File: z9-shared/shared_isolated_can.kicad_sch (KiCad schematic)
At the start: 6 parts, among them U951 ISO1042-Q1

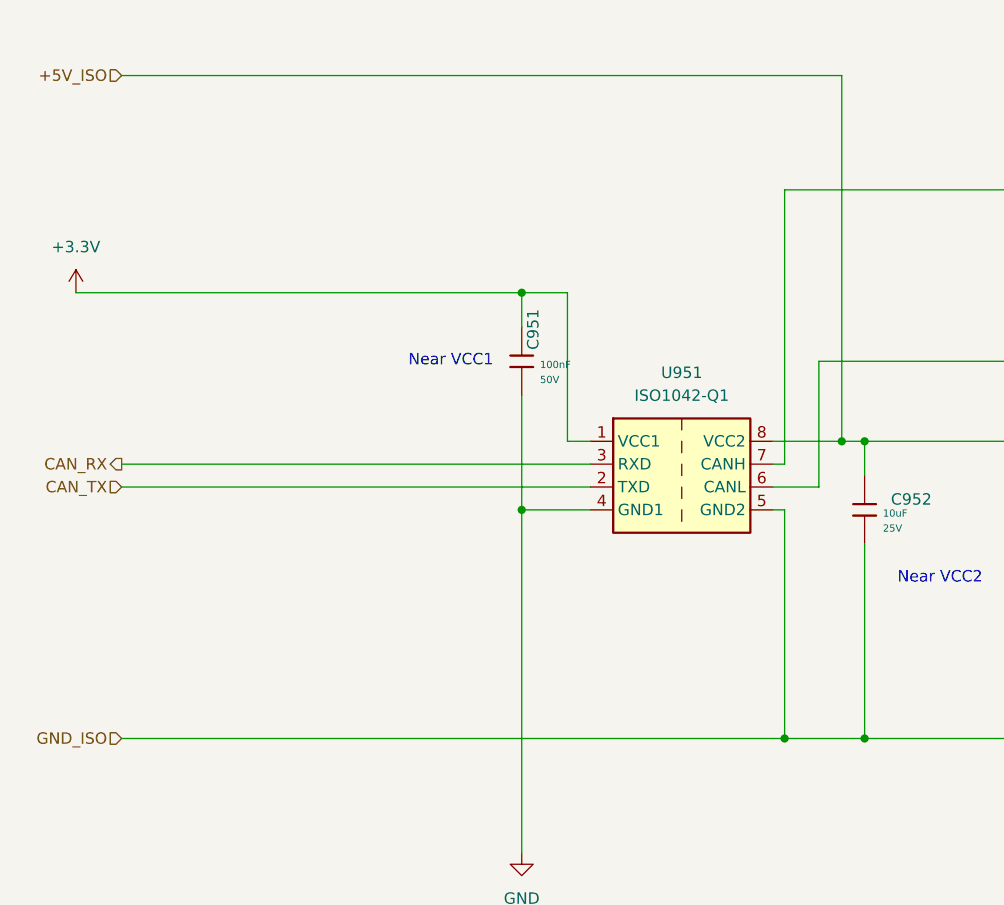
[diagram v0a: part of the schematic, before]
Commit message: Add PWR_FLAG symbols to schematic for power source indication
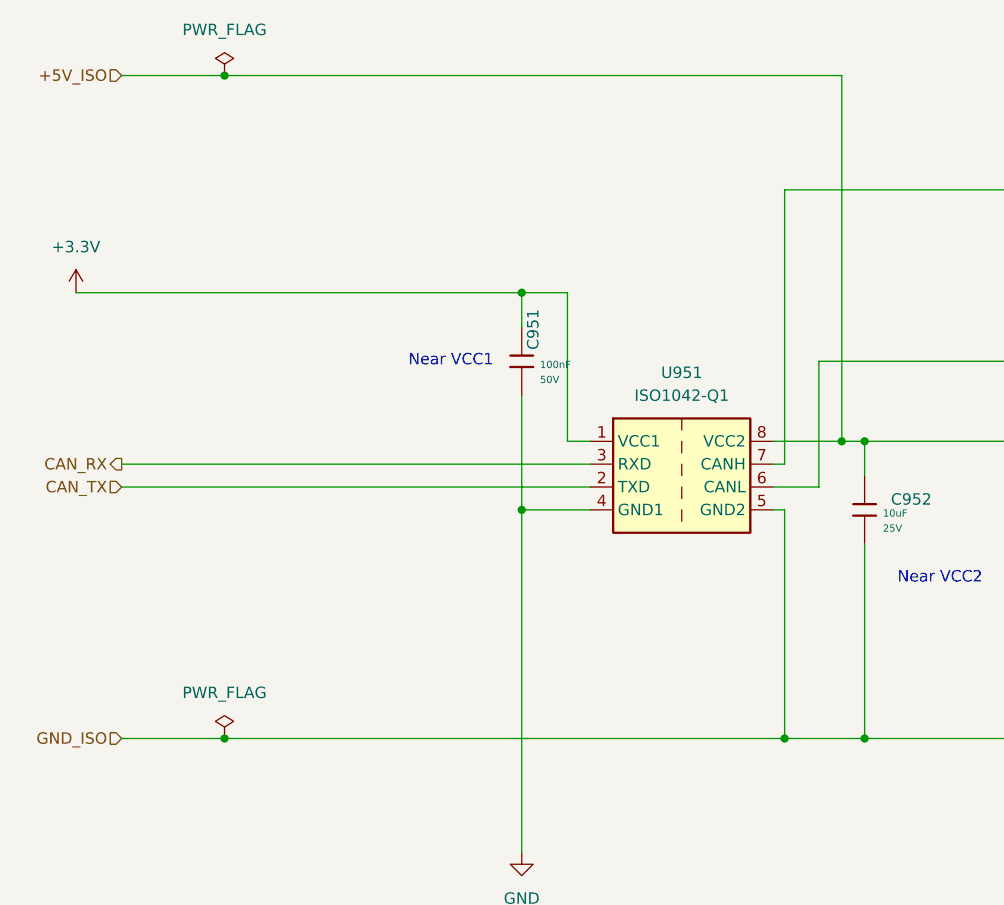
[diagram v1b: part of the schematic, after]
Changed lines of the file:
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@@
+	)
+	(junction
+		(at 95.25 49.53)
+		(diameter 0)
+		(color 0 0 0 0)
 	)
 	(junction
@@
 	)
 	(junction
+		(at 95.25 123.19)
+		(diameter 0)
+		(color 0 0 0 0)
+	)
+	(junction
 		(at 157.48 123.19)
 		(diameter 0)
@@
 	(wire
 		(pts
-			(xy 83.82 123.19) (xy 157.48 123.19)
+			(xy 95.25 49.53) (xy 163.83 49.53)
+		)
+		(stroke
+			(width 0)
+			(type default)
+		)
+	)
+	(wire
+		(pts
+			(xy 95.25 123.19) (xy 157.48 123.19)
+		)
+		(stroke
+			(width 0)
+			(type default)
+		)
+	)
+	(wire
+		(pts
+			(xy 83.82 123.19) (xy 95.25 123.19)
 		)
 		(stroke
@@
 	(wire
 		(pts
-			(xy 83.82 49.53) (xy 163.83 49.53)
+			(xy 83.82 49.53) (xy 95.25 49.53)
 		)
 		(stroke
@@
 	)
 	(symbol
+		(lib_id "power:PWR_FLAG")
+		(at 95.25 123.19 0)
+		(unit 1)
+		(exclude_from_sim no)
+		(in_bom yes)
+		(on_board yes)
+		(dnp no)
+		(fields_autoplaced yes)
+		(property "Reference" "#FLG0702"
+			(at 95.25 121.285 0)
+			(effects
+				(font
+					(size 1.27 1.27)
+				)
+				(hide yes)
+			)
+		)
+		(property "Value" "PWR_FLAG"
+			(at 95.25 118.11 0)
+			(effects
+				(font
+					(size 1.27 1.27)
+				)
+			)
+		)
+		(property "Footprint" ""
+			(at 95.25 123.19 0)
+			(effects
+				(font
+					(size 1.27 1.27)
+				)
+				(hide yes)
+			)
+		)
+		(property "Datasheet" "~"
+			(at 95.25 123.19 0)
+			(effects
+				(font
+					(size 1.27 1.27)
+				)
+				(hide yes)
+			)
+		)
+		(property "Description" "Special symbol for telling ERC where power comes from"
+			(at 95.25 123.19 0)
+			(effects
+				(font
+					(size 1.27 1.27)
+				)
+				(hide yes)
+			)
+		)
+		(pin "1"
+		)
+		(instances
+			(project "z9-console"
+				(path "/8d063f79-9282-4820-bcf4-1ff3c006cf08/f6275c7c-4728-4868-9630-23eeb36e7047"
+					(reference "#FLG0702")
+					(unit 1)
+				)
+			)
+		)
+	)
+	(symbol
 		(lib_id "power:+3.3V")
 		(at 78.74 73.66 0)
@@
 					(unit 1)
 				)
+			)
+		)
+	)
+	(symbol
+		(lib_id "power:PWR_FLAG")
+		(at 95.25 49.53 0)
+		(unit 1)
+		(exclude_from_sim no)
+		(in_bom yes)
+		(on_board yes)
+		(dnp no)
+		(fields_autoplaced yes)
+		(property "Reference" "#FLG0701"
+			(at 95.25 47.625 0)
+			(effects
+				(font
+					(size 1.27 1.27)
+				)
+				(hide yes)
+			)
+		)
+		(property "Value" "PWR_FLAG"
+			(at 95.25 44.45 0)
+			(effects
+				(font
+					(size 1.27 1.27)
+				)
+			)
+		)
+		(property "Footprint" ""
+			(at 95.25 49.53 0)
+			(effects
+				(font
+					(size 1.27 1.27)
+				)
+				(hide yes)
+			)
+		)
+		(property "Datasheet" "~"
+			(at 95.25 49.53 0)
+			(effects
+				(font
+					(size 1.27 1.27)
+				)
+				(hide yes)
+			)
+		)
+		(property "Description" "Special symbol for telling ERC where power comes from"
+			(at 95.25 49.53 0)
+			(effects
+				(font
+					(size 1.27 1.27)
+				)
+				(hide yes)
+			)
+		)
+		(pin "1"
+		)
+		(instances
+			(project ""
+				(path "/8d063f79-9282-4820-bcf4-1ff3c006cf08/f6275c7c-4728-4868-9630-23eeb36e7047"
+					(reference "#FLG0701")
+					(unit 1)
+				)

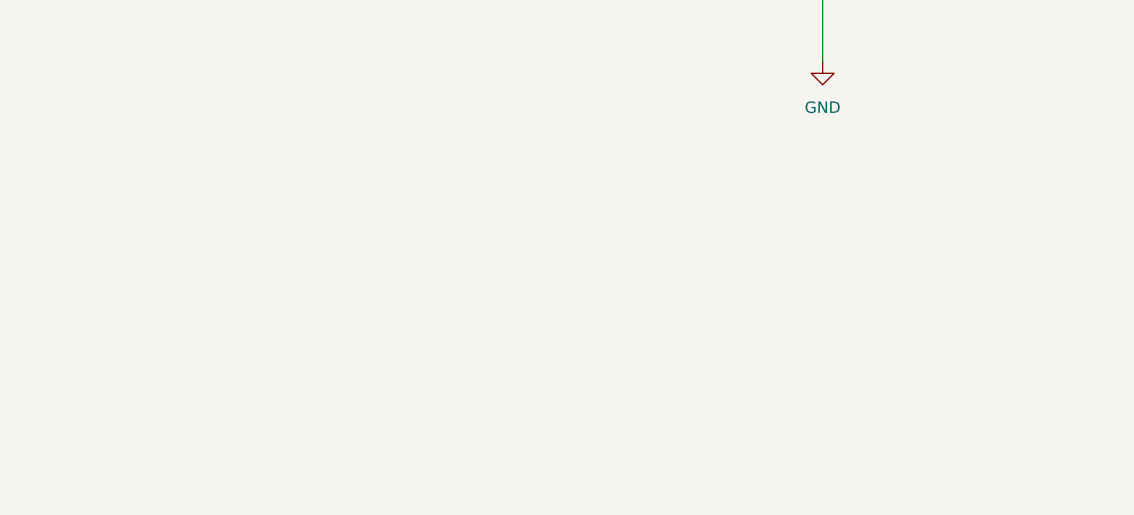
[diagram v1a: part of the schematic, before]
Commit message: Remove unused components and adjust annotation start number in project files
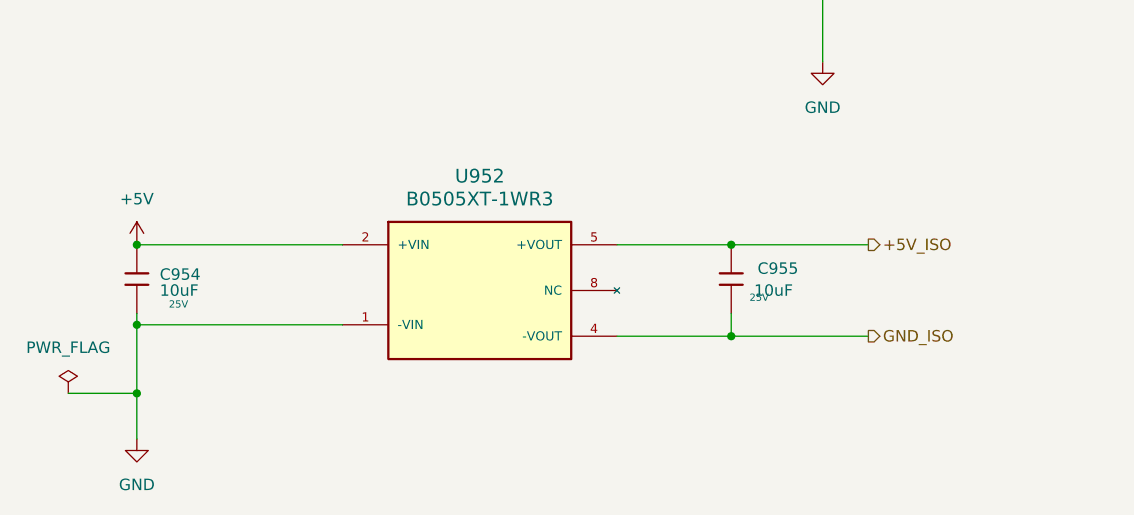
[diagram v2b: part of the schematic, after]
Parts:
- added C954, C955: 10uF, dnt:C_0603_1608Metric, symbol dnt_global:0603,10uF,_25V
- added U952: B0505XT-1WR3, dnt:B0505_Isolated_SMD, symbol dnt_global:B0505_Isolated_SMD
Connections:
- net +5V_ISO: now also C955.1, U952.5 (+VOUT)
- net GND: now also C954.2, U952.1 (-VIN)
- net GND_ISO: now also C955.2, U952.4 (-VOUT)
- new net +5V: C954.1, U952.2 (+VIN)

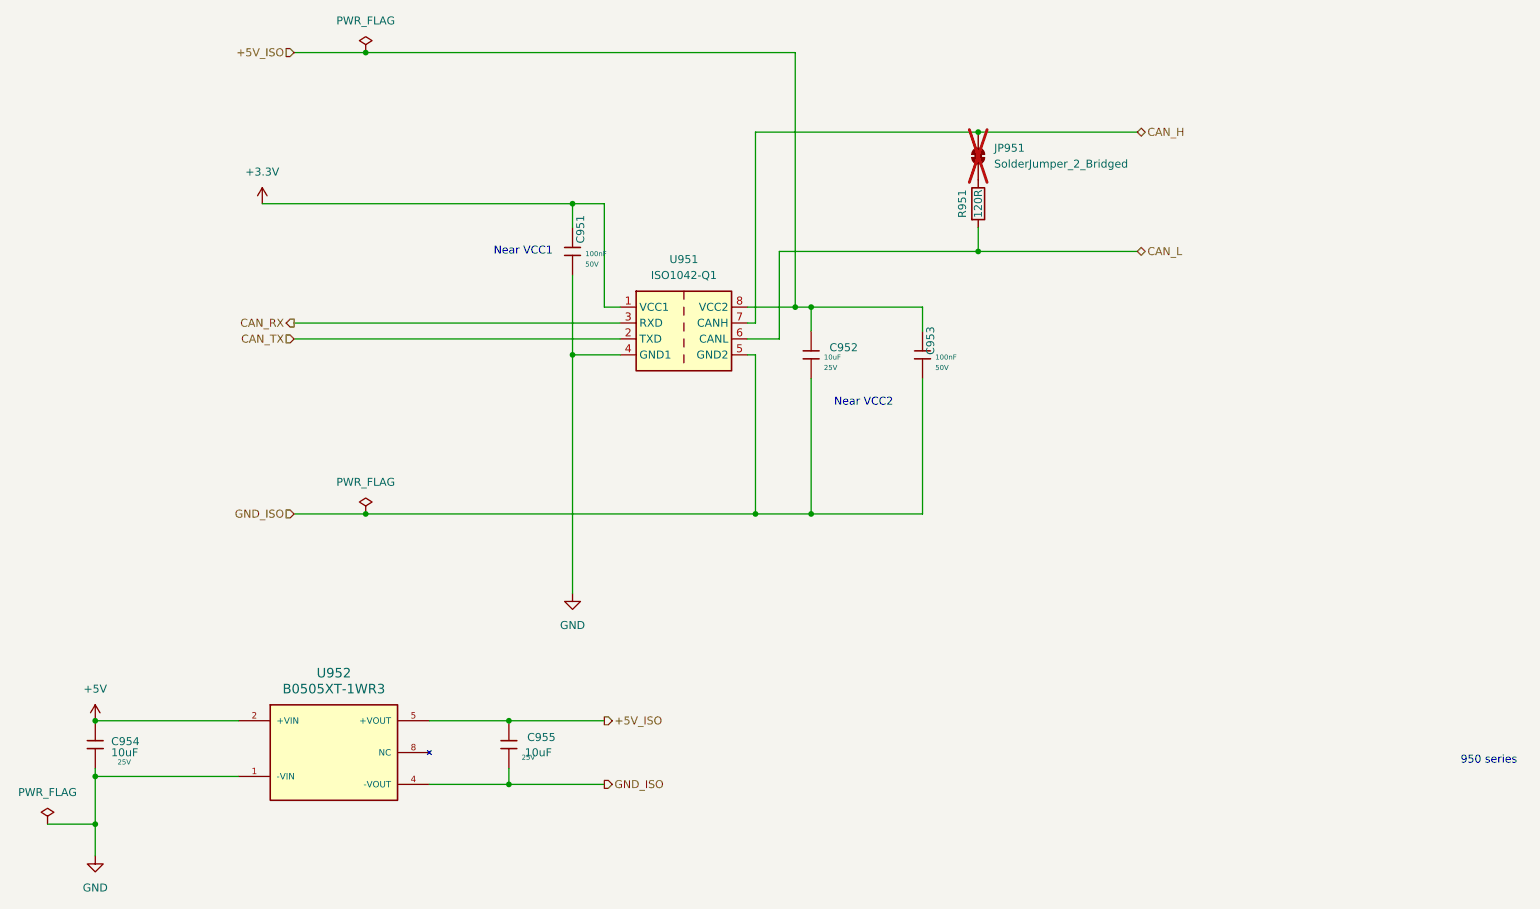
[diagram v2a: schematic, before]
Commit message: Update error handling for footprint and junction issues in project settings
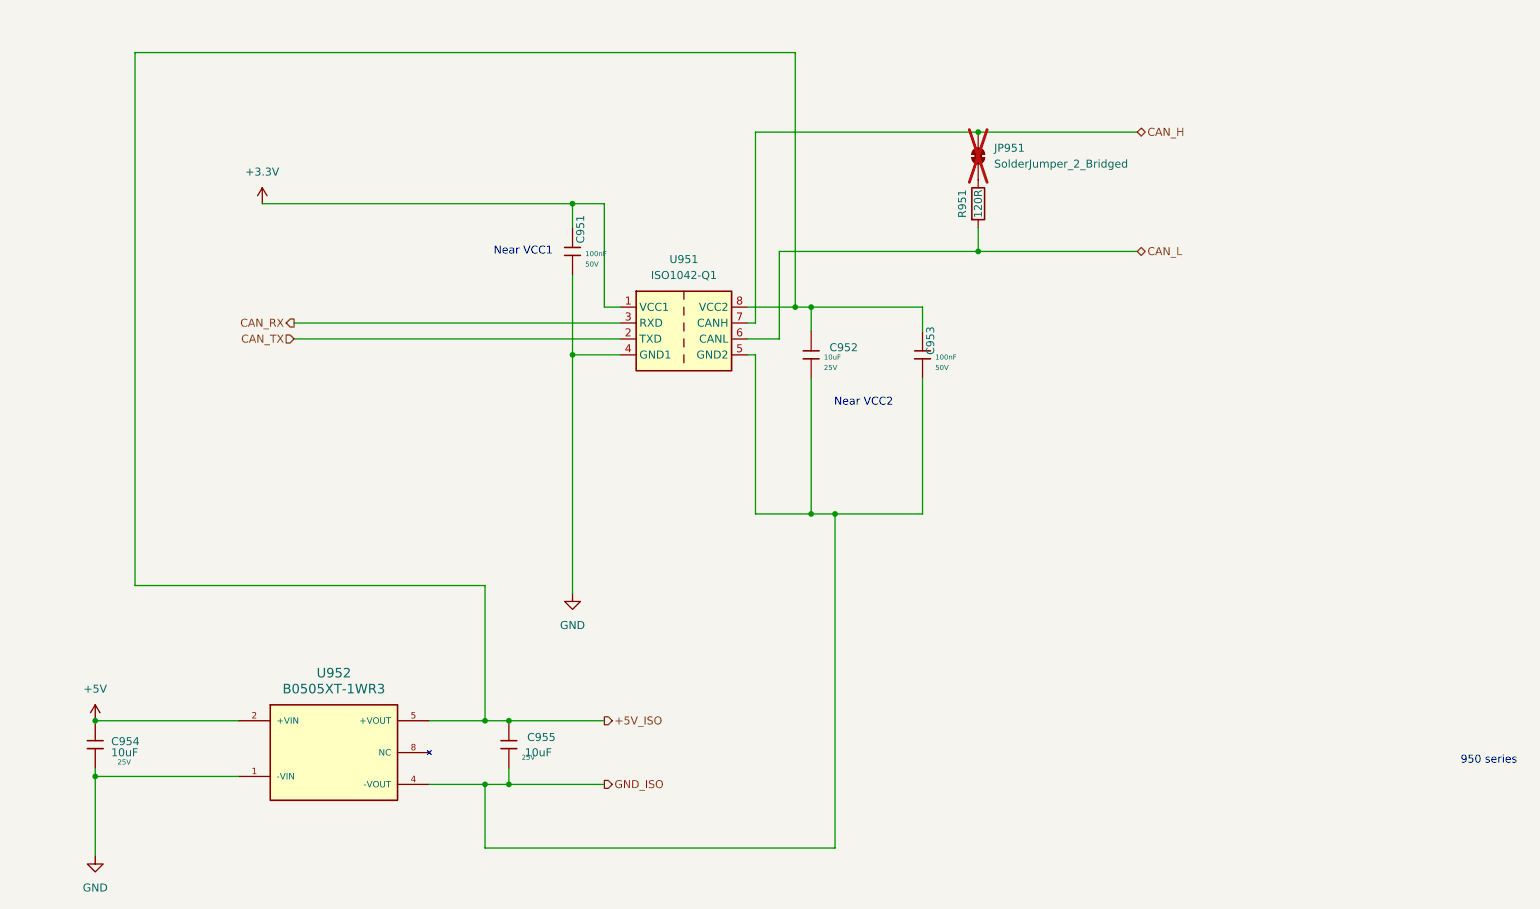
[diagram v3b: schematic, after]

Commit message: x
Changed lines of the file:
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@@
 		(instances
 			(project "z9-shared"
-				(path "/09e08bdc-786f-4949-8afc-e02ddbe0502e/0e53bd87-7ef1-4ffd-bb7a-214552c0f320"
-					(reference "#PWR0952")
+				(path "/09e08bdc-786f-4949-8afc-e02ddbe0502e/a613cbdc-c893-46e2-859f-3c7622690192"
+					(reference "#PWR0117")
 					(unit 1)
 				)
@@
 		(instances
 			(project "z9-shared"
-				(path "/09e08bdc-786f-4949-8afc-e02ddbe0502e/0e53bd87-7ef1-4ffd-bb7a-214552c0f320"
-					(reference "C953")
+				(path "/09e08bdc-786f-4949-8afc-e02ddbe0502e/a613cbdc-c893-46e2-859f-3c7622690192"
+					(reference "C?")
 					(unit 1)
 				)
@@
 		(instances
 			(project "z9-shared"
-				(path "/09e08bdc-786f-4949-8afc-e02ddbe0502e/0e53bd87-7ef1-4ffd-bb7a-214552c0f320"
-					(reference "#PWR0954")
+				(path "/09e08bdc-786f-4949-8afc-e02ddbe0502e/a613cbdc-c893-46e2-859f-3c7622690192"
+					(reference "#PWR0115")
 					(unit 1)
 				)
@@
 		(instances
 			(project "z9-shared"
-				(path "/09e08bdc-786f-4949-8afc-e02ddbe0502e/0e53bd87-7ef1-4ffd-bb7a-214552c0f320"
-					(reference "R951")
+				(path "/09e08bdc-786f-4949-8afc-e02ddbe0502e/a613cbdc-c893-46e2-859f-3c7622690192"
+					(reference "R?")
 					(unit 1)
 				)
@@
 		(instances
 			(project "z9-shared"
-				(path "/09e08bdc-786f-4949-8afc-e02ddbe0502e/0e53bd87-7ef1-4ffd-bb7a-214552c0f320"
-					(reference "C951")
+				(path "/09e08bdc-786f-4949-8afc-e02ddbe0502e/a613cbdc-c893-46e2-859f-3c7622690192"
+					(reference "C?")
 					(unit 1)
 				)
@@
 		(dnp no)
 		(property "Reference" "C955"
-			(at 121.031 158.8516 0)
+			(at 120.396 158.75 0)
 			(effects
 				(font
@@
 		)
 		(property "Value" "10uF"
-			(at 120.65 161.29 0)
+			(at 120.65 160.528 0)
 			(effects
 				(font
@@
 		)
 		(property "Voltage Rated" "25V"
-			(at 120.142 162.0662 0)
+			(at 120.904 162.052 0)
 			(effects
 				(font
@@
 		(instances
 			(project "z9-shared"
-				(path "/09e08bdc-786f-4949-8afc-e02ddbe0502e/0e53bd87-7ef1-4ffd-bb7a-214552c0f320"
-					(reference "C955")
+				(path "/09e08bdc-786f-4949-8afc-e02ddbe0502e/a613cbdc-c893-46e2-859f-3c7622690192"
+					(reference "C?")
 					(unit 1)
 				)
@@
 		(instances
 			(project "z9-shared"
-				(path "/09e08bdc-786f-4949-8afc-e02ddbe0502e/0e53bd87-7ef1-4ffd-bb7a-214552c0f320"
-					(reference "C952")
+				(path "/09e08bdc-786f-4949-8afc-e02ddbe0502e/a613cbdc-c893-46e2-859f-3c7622690192"
+					(reference "C?")
 					(unit 1)
 				)
@@
 		(instances
 			(project "z9-shared"
-				(path "/09e08bdc-786f-4949-8afc-e02ddbe0502e/0e53bd87-7ef1-4ffd-bb7a-214552c0f320"
-					(reference "#PWR0951")
+				(path "/09e08bdc-786f-4949-8afc-e02ddbe0502e/a613cbdc-c893-46e2-859f-3c7622690192"
+					(reference "#PWR0114")
 					(unit 1)
 				)
@@
 		(instances
 			(project "z9-shared"
-				(path "/09e08bdc-786f-4949-8afc-e02ddbe0502e/0e53bd87-7ef1-4ffd-bb7a-214552c0f320"
-					(reference "C954")
+				(path "/09e08bdc-786f-4949-8afc-e02ddbe0502e/a613cbdc-c893-46e2-859f-3c7622690192"
+					(reference "C?")
 					(unit 1)
 				)
@@
 		(instances
 			(project "z9-shared"
-				(path "/09e08bdc-786f-4949-8afc-e02ddbe0502e/0e53bd87-7ef1-4ffd-bb7a-214552c0f320"
-					(reference "#PWR0955")
+				(path "/09e08bdc-786f-4949-8afc-e02ddbe0502e/a613cbdc-c893-46e2-859f-3c7622690192"
+					(reference "#PWR0116")
 					(unit 1)
 				)
@@
 		(instances
 			(project "z9-shared"
-				(path "/09e08bdc-786f-4949-8afc-e02ddbe0502e/0e53bd87-7ef1-4ffd-bb7a-214552c0f320"
-					(reference "U952")
+				(path "/09e08bdc-786f-4949-8afc-e02ddbe0502e/a613cbdc-c893-46e2-859f-3c7622690192"
+					(reference "U?")
 					(unit 1)
 				)
@@
 		(instances
 			(project "z9-shared"
-				(path "/09e08bdc-786f-4949-8afc-e02ddbe0502e/0e53bd87-7ef1-4ffd-bb7a-214552c0f320"
-					(reference "JP951")
+				(path "/09e08bdc-786f-4949-8afc-e02ddbe0502e/a613cbdc-c893-46e2-859f-3c7622690192"
+					(reference "JP?")
 					(unit 1)
 				)
@@
 		(instances
 			(project "z9-shared"
-				(path "/09e08bdc-786f-4949-8afc-e02ddbe0502e/0e53bd87-7ef1-4ffd-bb7a-214552c0f320"
-					(reference "U951")
-					(unit 1)
-				)
+				(path "/09e08bdc-786f-4949-8afc-e02ddbe0502e/a613cbdc-c893-46e2-859f-3c7622690192"
+					(reference "U?")
+					(unit 1)
+				)
